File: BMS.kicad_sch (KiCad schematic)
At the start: 1 part, among them Q1 IRFS4229

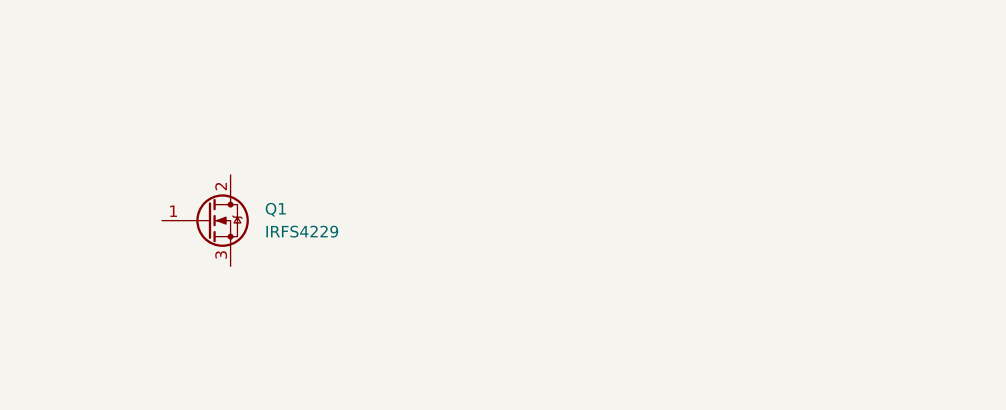
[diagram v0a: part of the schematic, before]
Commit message: finish battery terminal placement
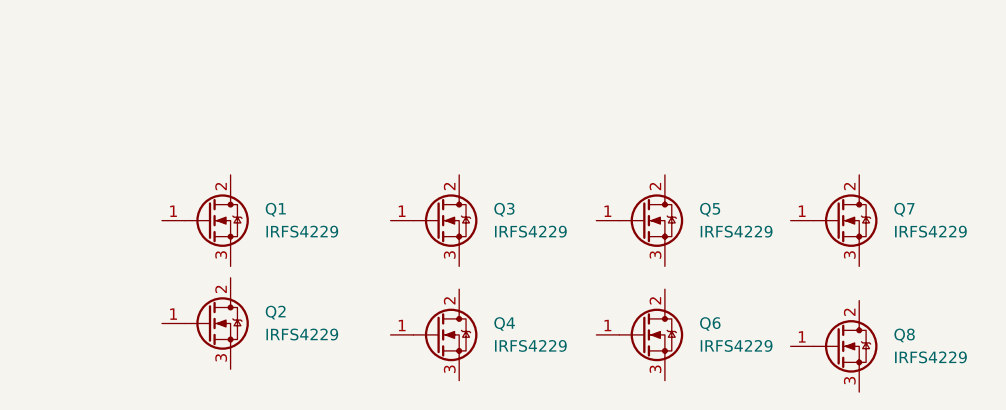
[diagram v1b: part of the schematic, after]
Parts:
- added Q2, Q3, Q4, Q5, Q6, Q7, Q8: IRFS4229, Package_TO_SOT_SMD:TO-263-2, symbol Transistor_FET:IRFS4229
